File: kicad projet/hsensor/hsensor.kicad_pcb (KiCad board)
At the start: 2 copper layers, 3 parts, among them U1 TLV75801PDBV, U2 TLV75801PDBV

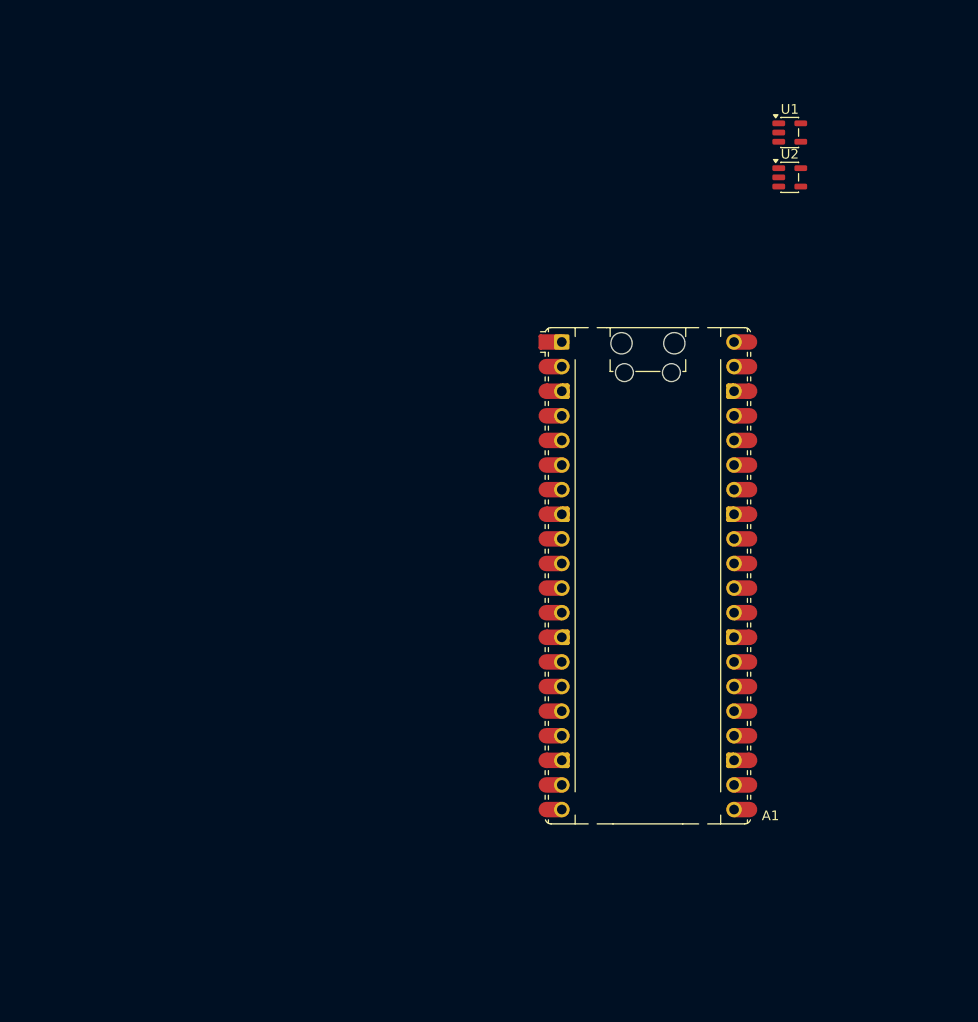
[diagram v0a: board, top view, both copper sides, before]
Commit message: updated schematics
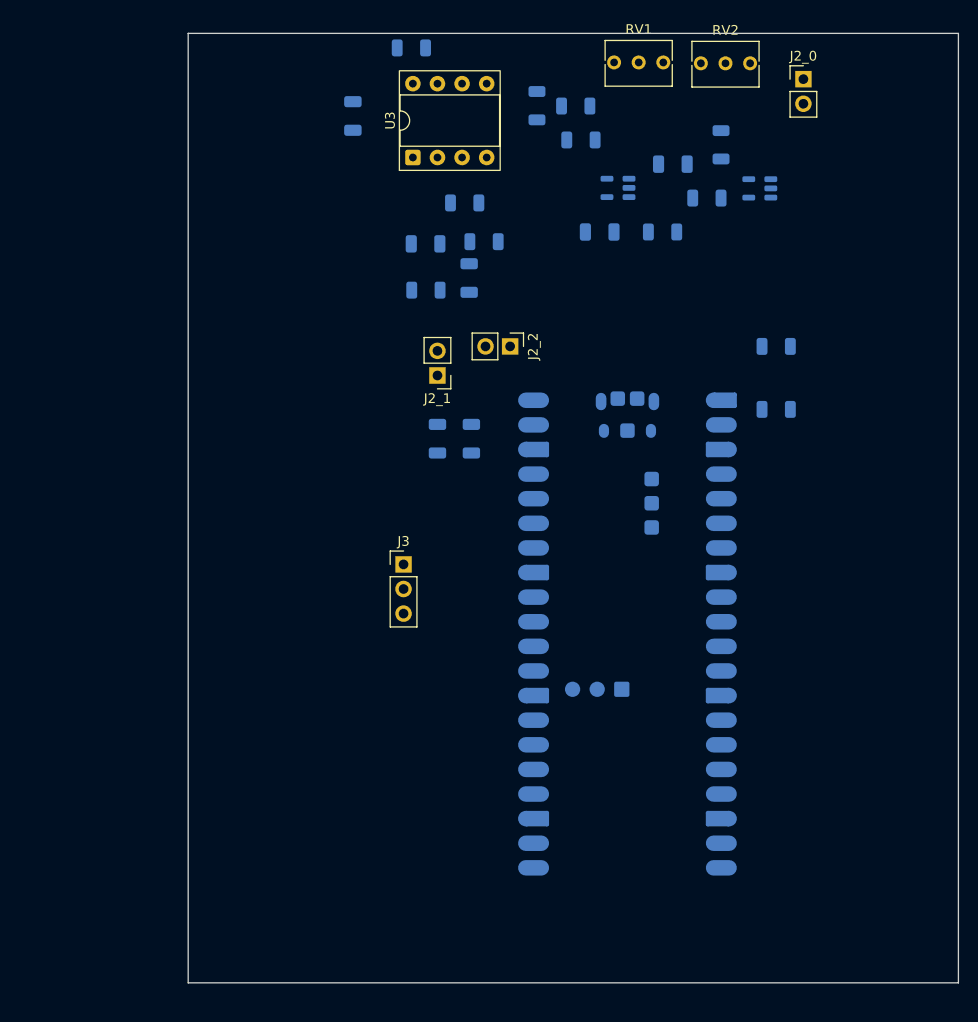
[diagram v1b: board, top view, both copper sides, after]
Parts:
- added C1: C, Capacitor_SMD:C_1206_3216Metric, B.Cu at (152.3, 74.4)
- added C2: 68e-9, Capacitor_SMD:C_1206_3216Metric, B.Cu at (147.8, 70.9)
- added C3: 2.2e-6, Capacitor_SMD:C_1206_3216Metric, B.Cu at (140.3, 57.7)
- added C4: 1e-6, Capacitor_SMD:C_1206_3216Metric, B.Cu at (165.7, 69.7)
- added C5: 10e-6, Capacitor_SMD:C_1206_3216Metric, B.Cu at (173.3, 62.7)
- added C6: 1e-6, Capacitor_SMD:C_1206_3216Metric, B.Cu at (152.5, 91.0)
- added C7: 10e-6, Capacitor_SMD:C_1206_3216Metric, B.Cu at (149.0, 91.0)
- added J2_0: Conn_01x02_Pin, Connector_PinHeader_2.54mm:PinHeader_1x02_P2.54mm_Vertical, F.Cu at (186.8, 53.9)
- added J2_1: Conn_01x02_Pin, Connector_PinHeader_2.54mm:PinHeader_1x02_P2.54mm_Vertical, F.Cu at (149.0, 84.5)
- added J2_2: Conn_01x02_Pin, Connector_PinHeader_2.54mm:PinHeader_1x02_P2.54mm_Vertical, F.Cu at (156.5, 81.5)
- added J3: Conn_01x03_Pin, Connector_PinHeader_2.54mm:PinHeader_1x03_P2.54mm_Vertical, F.Cu at (145.5, 104.0)
- added R10: 4.7e3, Resistor_SMD:R_1206_3216Metric, B.Cu at (172.2, 69.7)
- added R11: 10e3, Resistor_SMD:R_1206_3216Metric, B.Cu at (163.8, 60.2)
- added R3: 100e3, Resistor_SMD:R_1206_3216Metric, B.Cu at (153.8, 70.7)
- added R4: 10e3, Resistor_SMD:R_1206_3216Metric, B.Cu at (151.8, 66.7)
- added R5: 680e3, Resistor_SMD:R_1206_3216Metric, B.Cu at (147.8, 75.7)
- added R6: 100e3, Resistor_SMD:R_1206_3216Metric, B.Cu at (146.3, 50.7)
- added R7: 10e3, Resistor_SMD:R_1206_3216Metric, B.Cu at (159.3, 56.7)
- added R8: 5.6e3, Resistor_SMD:R_1206_3216Metric, B.Cu at (176.8, 66.2)
- added R9: 36e3, Resistor_SMD:R_1206_3216Metric, B.Cu at (178.3, 60.7)
- added RV1: 100e3, Potentiometer_THT:Potentiometer_Bourns_3266Y_Vertical, F.Cu at (172.3, 52.2)
- added RV2: 5.e3, Potentiometer_THT:Potentiometer_Bourns_3266Y_Vertical, F.Cu at (181.3, 52.3)
- added RV3: 5e3, Resistor_SMD:R_1206_3216Metric, B.Cu at (163.3, 56.7)
- added Rsens1: R, Resistor_SMD:R_1206_3216Metric, B.Cu at (184.0, 81.5)
- added Rsens2: R, Resistor_SMD:R_1206_3216Metric, B.Cu at (184.0, 88.0)
- added U3: LM358, Package_DIP:DIP-8_W7.62mm_Socket, F.Cu at (146.5, 62.0)
- A1: footprint Module:RaspberryPi_Pico_Common_Unspecified -> Module:RaspberryPi_Pico_W_SMD; moved to B.Cu
- U1, U2: moved to B.Cu
- moved U2 17.8 mm to (167.6, 65.1), turned to 180 degrees
- moved U1 6.54 mm to (182.3, 65.2), turned to 180 degrees
- moved A1 6.38 mm to (168.6, 111.2), turned to 180 degrees
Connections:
- A1 pad 31: Net-(A1-GPIO26_ADC0) -> Raspberry_ADC
- A1 pad 33: GND -> unconnected-(A1-AGND-Pad33)
- A1 pad 39: unconnected-(A1-VSYS-Pad39) -> Vsup
- U1 pad 1: /Vsup -> Vsup
- U1 pad 3: /Vsup -> Vsup
- U2 pad 1: /Vsup -> Vsup
- U2 pad 3: /Vsup -> Vsup
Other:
- board outline added: 79.5 x 98 mm

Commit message: final pcb (i hope)
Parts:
- added U4: TCRT5000, Sensor:OPTO_TCRT5000, F.Cu at (140.8, 142.7)
- A1: footprint Module:RaspberryPi_Pico_W_SMD -> Module:RaspberryPi_Pico_Common_THT; moved to F.Cu
- RV3: value 5e3 -> 5.e3; footprint Resistor_SMD:R_1206_3216Metric -> Potentiometer_THT:Potentiometer_Bourns_3266Y_Vertical; moved to F.Cu
- moved Rsens1 67.5 mm to (138.0, 131.0), turned to -90 degrees
- moved RV1 64.6 mm to (138.0, 106.9), turned to 90 degrees
- moved C3 62.3 mm to (141.8, 120.0)
- moved U3 61.8 mm to (145.6, 123.8), turned to 180 degrees
- moved J2_0 58.4 mm to (138.6, 87.0), turned to -90 degrees
- moved Rsens2 58.0 mm to (141.5, 127.5), turned to 0 degrees
- moved RV2 57.5 mm to (137.8, 89.9), turned to 90 degrees
- moved R6 53.4 mm to (138.3, 103.5)
- moved R4 53.3 mm to (150.8, 120.0), turned to 90 degrees
- moved C2 52.6 mm to (149.8, 123.5)
- moved R5 51.9 mm to (149.8, 127.5)
- moved R11 51.6 mm to (147.0, 109.0)
- moved RV3 49.8 mm to (147.7, 103.9), turned to 0 degrees
- moved J2_2 48.1 mm to (154.0, 129.5), turned to 180 degrees
- moved R7 47.6 mm to (138.5, 99.5), turned to 0 degrees
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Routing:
- net Vsup: track 0.00 -> 63.2 mm, vias 0 -> 2
- net VDD: track 0.00 -> 49.1 mm
- net Net-(U3B--): track 0.00 -> 31.6 mm, vias 0 -> 2
- net VCM: track 0.00 -> 29.3 mm
- net Raspberry_ADC: track 0.00 -> 27.9 mm
- net Net-(J3-Pin_1): track 0.00 -> 27.6 mm
- net Sensor: track 0.00 -> 26.3 mm, vias 0 -> 2
- net Net-(U3B-+): track 0.00 -> 21.8 mm
- net Net-(J2_0-Pin_1): track 0.00 -> 21.7 mm
- net Net-(J2_2-Pin_2): track 0.00 -> 15.7 mm
- net GND: track 0.00 -> 14.7 mm
- net Net-(Rsens2-Pad2): track 0.00 -> 14.2 mm
- net Net-(C2-Pad1): track 0.00 -> 11.1 mm
- net Net-(U3A--): track 0.00 -> 11.0 mm
- net Net-(J2_1-Pin_1): track 0.00 -> 9.73 mm
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- added copper zone on B.Cu, net GND
- added copper zone on F.Cu, net GND
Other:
- board size 79.5 x 98 mm -> 63.3 x 70.6 mm
- board text added: "MARC F GASP V"
- board text added: "PETIT PET"

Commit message: added demo files
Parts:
- moved C5 21.9 mm to (131.9, 78.6)
- moved C6 21.9 mm to (135.1, 78.7)
- moved R8 21.9 mm to (129.2, 78.6)
- moved C1 21.3 mm to (130.2, 104.1)
- moved C2 21.3 mm to (130.2, 115.1)
- moved C3 21.3 mm to (122.2, 111.6)
- moved C4 21.3 mm to (132.4, 90.1)
- moved C7 21.3 mm to (132.2, 93.1)
- moved J2_0 21.3 mm to (119.0, 78.6)
- moved J2_1 21.3 mm to (127.0, 91.1)
- moved R10 21.3 mm to (132.2, 100.6)
- moved R11 21.3 mm to (127.4, 100.6)
- moved R3 21.3 mm to (129.7, 107.1)
- moved R5 21.3 mm to (130.2, 119.1)
- moved R7 21.3 mm to (118.9, 91.1)
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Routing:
- net Vsup: track 63.2 -> 96.2 mm, vias 2 -> 5
- net Net-(J3-Pin_1): track 27.6 -> 33.1 mm
- net Net-(U3B--): track 31.6 -> 26.2 mm, vias 2 -> 0
- net VCM: track 29.3 -> 33.2 mm, vias 0 -> 2
- net Raspberry_ADC: track 27.9 -> 31.2 mm
- net GND: track 14.7 -> 17.9 mm
- net Net-(U3A--): track 11.0 -> 13.0 mm
- net Net-(U1-FB): track 7.69 -> 9.61 mm
- net Net-(J2_0-Pin_1): track 21.7 -> 22.6 mm, vias 0 -> 2
- net Net-(U3B-+): track 21.8 -> 21.2 mm
